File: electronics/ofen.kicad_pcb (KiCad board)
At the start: 2 copper layers, 100.3 x 76.2 mm, 61 parts, among them J1 motor, J2 DC, J3 AC_IN, J4 AC_OUT, J5 AC_OUT, Q1 Q_NPN_CBE, Q2 Q_NPN_CBE, Q3 Q_NPN_CBE, Q4 Q_NPN_CBE, Q5 BTA16-600B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

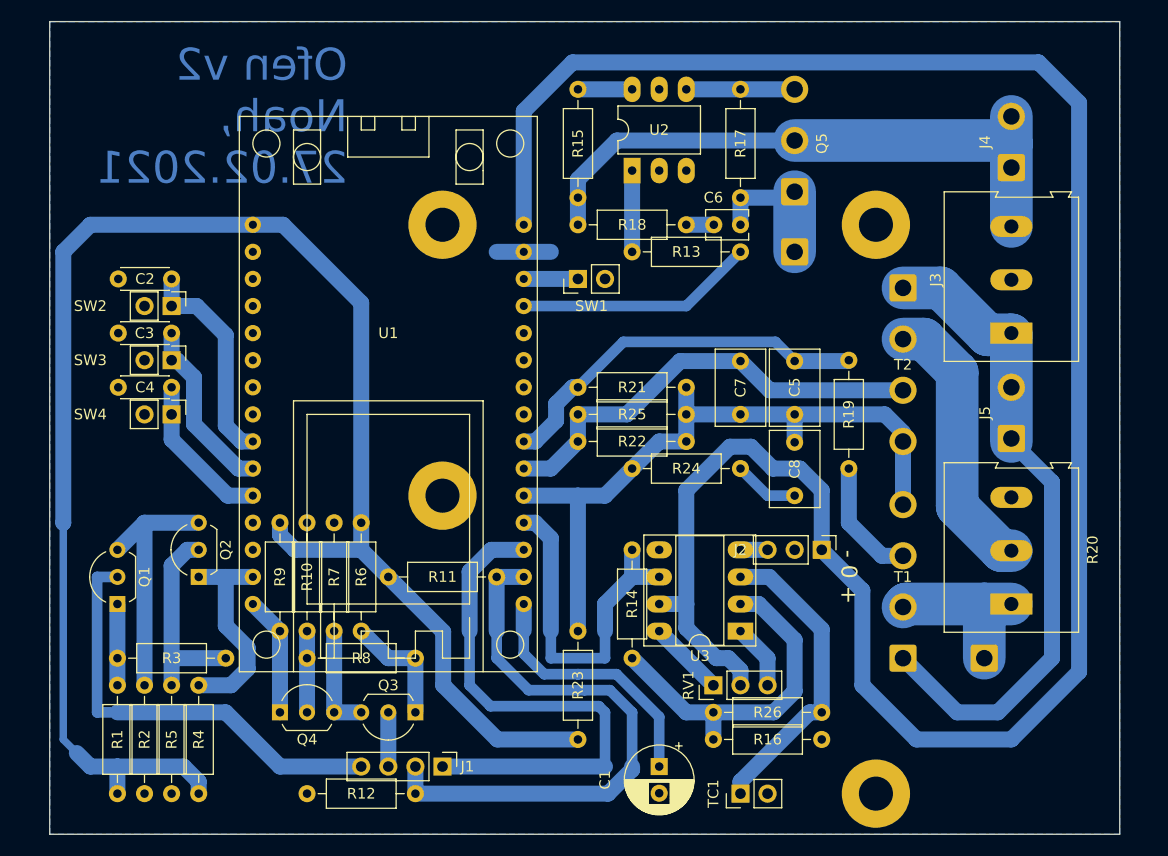
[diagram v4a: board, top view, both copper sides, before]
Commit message: added cold junction compensation and three status leds
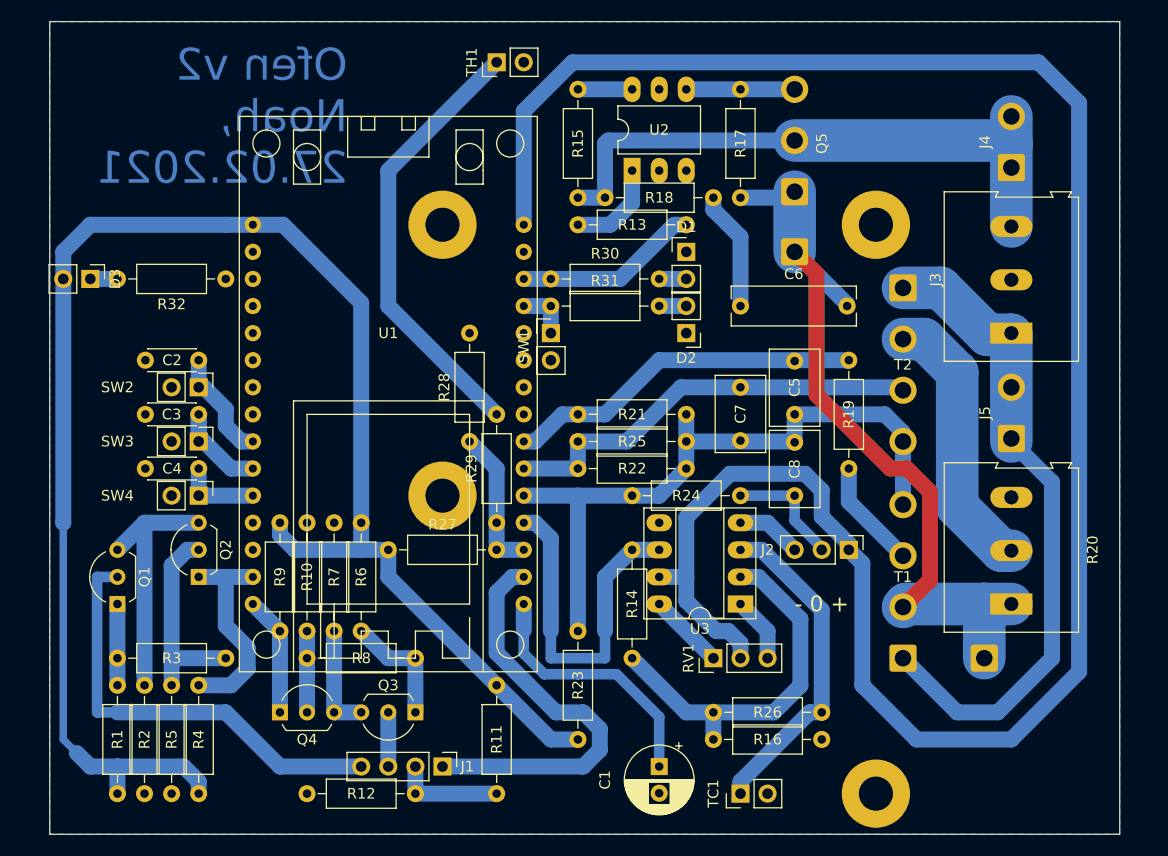
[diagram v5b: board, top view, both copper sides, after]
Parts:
- added D1: LED_heating, Connector_PinHeader_2.54mm:PinHeader_1x02_P2.54mm_Vertical, F.Cu at (177.8, 78.7)
- added D2: LED_running, Connector_PinHeader_2.54mm:PinHeader_1x02_P2.54mm_Vertical, F.Cu at (177.8, 86.4)
- added D3: LED_on, Connector_PinHeader_2.54mm:PinHeader_1x02_P2.54mm_Vertical, F.Cu at (121.9, 81.3)
- added R27: 15k, Resistor_THT:R_Axial_DIN0207_L6.3mm_D2.5mm_P10.16mm_Horizontal, F.Cu at (149.9, 106.7)
- added R28: 6.8k, Resistor_THT:R_Axial_DIN0207_L6.3mm_D2.5mm_P10.16mm_Horizontal, F.Cu at (157.5, 96.5)
- added R29: 330, Resistor_THT:R_Axial_DIN0207_L6.3mm_D2.5mm_P10.16mm_Horizontal, F.Cu at (160.0, 104.1)
- added R30: 68, Resistor_THT:R_Axial_DIN0207_L6.3mm_D2.5mm_P10.16mm_Horizontal, F.Cu at (165.1, 81.3)
- added R31: 68, Resistor_THT:R_Axial_DIN0207_L6.3mm_D2.5mm_P10.16mm_Horizontal, F.Cu at (165.1, 83.8)
- added R32: 68, Resistor_THT:R_Axial_DIN0207_L6.3mm_D2.5mm_P10.16mm_Horizontal, F.Cu at (134.6, 81.3)
- added TH1: 100k, Connector_PinHeader_2.54mm:PinHeader_1x02_P2.54mm_Vertical, F.Cu at (160.0, 61.0)
- C6: footprint Capacitor_THT:C_Disc_D3.8mm_W2.6mm_P2.50mm -> Capacitor_THT:C_Rect_L11.5mm_W3.5mm_P10.00mm_MKT
- R26: value 15k -> 3.3k
- moved R11 14.4 mm to (160.0, 119.4), turned to 270 degrees
- moved SW2 8.03 mm to (132.1, 91.4)
- moved C2 8.03 mm to (127.1, 88.9)
- moved C3 8.03 mm to (127.1, 94.0)
- moved C4 8.03 mm to (127.1, 99.1)
- moved SW3 8.03 mm to (132.1, 96.5)
- moved SW4 8.03 mm to (132.1, 101.6)
- moved C6 8.02 mm to (182.9, 83.8)
- moved R13 5.68 mm to (167.6, 76.2)
- moved SW1 5.68 mm to (165.1, 86.4), turned to 0 degrees
- moved R18 3.59 mm to (170.2, 73.7)
- moved R21 2.54 mm to (167.6, 94.0)
- moved R22 2.54 mm to (177.8, 99.1)
- moved J2 2.54 mm to (193.0, 106.7)
- moved R24 2.54 mm to (172.7, 101.6)
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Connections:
- SW1 pad 1: Net-(SW1-Pad1) -> Net-(R31-Pad1)
- U1 pad 17: Net-(J1-Pad2) -> Net-(J1-Pad1)
- U1 pad 18: Net-(J1-Pad1) -> Net-(R27-Pad2)
- U1 pad 27: Net-(R13-Pad2) -> Net-(R31-Pad1)
- U1 pad 28: Net-(SW1-Pad1) -> Net-(R13-Pad2)
- U1 pad 3: GND -> Net-(U1-Pad3)
- U1 pad 4: GND -> Net-(U1-Pad4)
- U1 pad 5: GND -> Net-(U1-Pad5)
- U1 pad 8: Net-(U1-Pad8) -> GND
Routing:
- net Net-(C6-Pad2): track 28.8 -> 73.9 mm
- net Net-(J1-Pad2): track 54.1 -> 10.2 mm
- net Net-(R29-Pad2): track 0.00 -> 41.4 mm
- net Net-(R27-Pad2): track 0.00 -> 13.8 mm
- net Net-(J1-Pad1): track 50.7 -> 38.8 mm
- net Net-(C2-Pad2): track 20.4 -> 10.6 mm
- net Net-(C6-Pad1): track 2.58 -> 11.2 mm
- net Net-(C4-Pad2): track 14.7 -> 7.62 mm
- net +5V: track 204.1 -> 198.0 mm
- net Net-(C3-Pad2): track 16.9 -> 10.9 mm
- net Net-(R31-Pad1): track 0.00 -> 5.08 mm
- net Net-(R13-Pad2): track 22.4 -> 17.3 mm
- net Net-(SW1-Pad1): track 5.08 -> 0.00 mm
- net -5V: track 2.54 -> 6.13 mm
- net Net-(R14-Pad1): track 32.0 -> 35.0 mm
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
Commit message: redesigned PCB. smaller, better, double layer
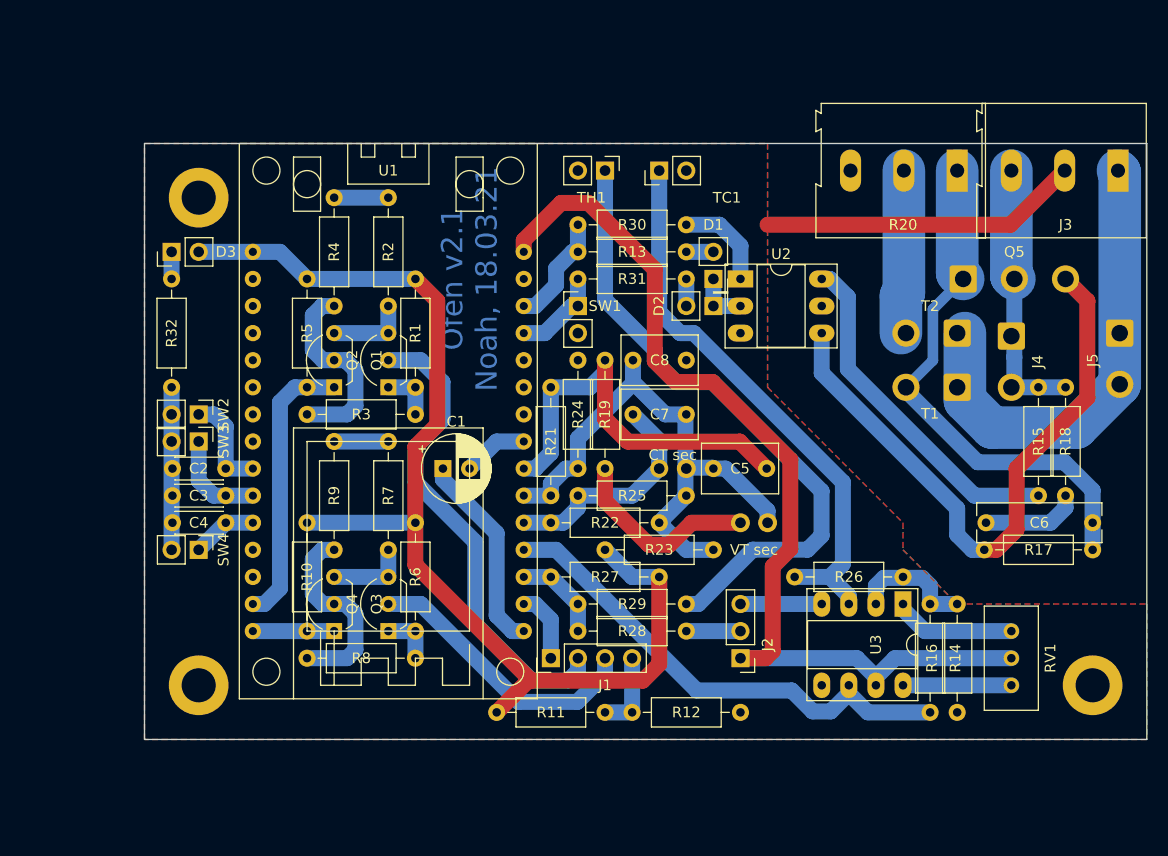
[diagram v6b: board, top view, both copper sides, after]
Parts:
- removed the   at (195.6, 129.5)
- removed the   at (154.9, 101.6)
- removed the   at (154.9, 76.2)
- removed the   at (195.6, 76.2)
- removed the   at (205.7, 116.8)
- removed the   at (188.0, 78.7)
- added  : , MountingHole:MountingHole_3.2mm_M3_DIN965_Pad, F.Cu at (132.1, 73.7)
- added  : , MountingHole:MountingHole_3.2mm_M3_DIN965_Pad, F.Cu at (215.9, 119.4)
- added  : , MountingHole:MountingHole_3.2mm_M3_DIN965_Pad, F.Cu at (132.1, 119.4)
- added ?: , , F.Cu at (182.9, 106.7)
- RV1: footprint Connector_PinHeader_2.54mm:PinHeader_1x03_P2.54mm_Vertical -> Potentiometer_THT:Potentiometer_Bourns_3296W_Vertical
- U2: footprint Package_DIP:DIP-6_W7.62mm_LongPads -> Package_DIP:DIP-6_W7.62mm_Socket_LongPads
- moved TC1 58.9 mm to (175.3, 71.1)
- moved R1 55.8 mm to (152.4, 81.3), turned to 270 degrees
- moved R5 49.3 mm to (142.2, 81.3), turned to 270 degrees
- moved R17 46.7 mm to (215.9, 106.7), turned to 180 degrees
- moved R15 46.7 mm to (210.8, 91.4), turned to 270 degrees
- moved R18 46.7 mm to (213.4, 91.4), turned to 270 degrees
- moved R2 42.3 mm to (149.9, 83.8), turned to 90 degrees
- moved R20 41.0 mm to (203.2, 71.1), turned to 180 degrees
- moved R4 38.7 mm to (144.8, 83.8), turned to 90 degrees
- moved C1 34.5 mm to (155.0, 99.1), turned to 0 degrees
- moved Q1 32.5 mm to (149.9, 91.4)
- moved C6 30.7 mm to (205.9, 104.1)
- moved R14 28.4 mm to (200.7, 111.8), turned to 270 degrees
- moved RV1 28.1 mm to (208.3, 119.4), turned to 270 degrees
- moved T1 25.9 mm to (203.2, 91.4), turned to 180 degrees
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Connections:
- Q1 pad 2: Net-(J1-Pad4) -> Net-(J1-Pad2)
- R11 pad 2: Net-(J1-Pad2) -> Net-(J1-Pad4)
- R12 pad 1: Net-(J1-Pad2) -> Net-(J1-Pad4)
- U1 pad 20: Net-(C5-Pad1) -> Net-(C7-Pad2)
- U1 pad 21: Net-(C7-Pad2) -> Net-(C5-Pad1)
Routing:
- net +5V: track 198.0 -> 92.1 mm
- net GND: track 11.2 -> 71.7 mm
- net +3V3: track 157.4 -> 106.8 mm
- net Net-(Q5-Pad3): track 10.2 -> 58.2 mm
- net Net-(J1-Pad2): track 10.2 -> 45.4 mm
- net Net-(J1-Pad4): track 40.8 -> 7.62 mm
- net Net-(J1-Pad1): track 38.8 -> 6.76 mm
- net Net-(J3-Pad3): track 56.3 -> 25.6 mm
- net Net-(R15-Pad2): track 5.08 -> 32.7 mm
- net Net-(C6-Pad2): track 73.9 -> 50.0 mm
- net Net-(R14-Pad1): track 35.0 -> 11.7 mm
- net Net-(R26-Pad2): track 31.0 -> 53.1 mm
- net Net-(J1-Pad3): track 5.08 -> 26.7 mm
- net Net-(C7-Pad2): track 40.3 -> 21.6 mm
- net Net-(R29-Pad2): track 41.4 -> 60.0 mm
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- added copper zone on F.Cu, net GND
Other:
- board size 100.3 x 76.2 mm -> 94 x 55.9 mm
- net class GND added: clearance 0.8, trace_width 0.7, via_dia 0.8, via_drill 0.4
- net class dick removed
- net class dünn removed
- net class mittel removed
- board text added: "CT sec"
- board text added: "Ofen v2.1 Noah, 18.03.21"
- board text added: "VT sec"
- board text removed: "- 0 +"
- board text removed: "Ofen v2 Noah, 27.02.2021"

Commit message: removed front GND pour on PCB
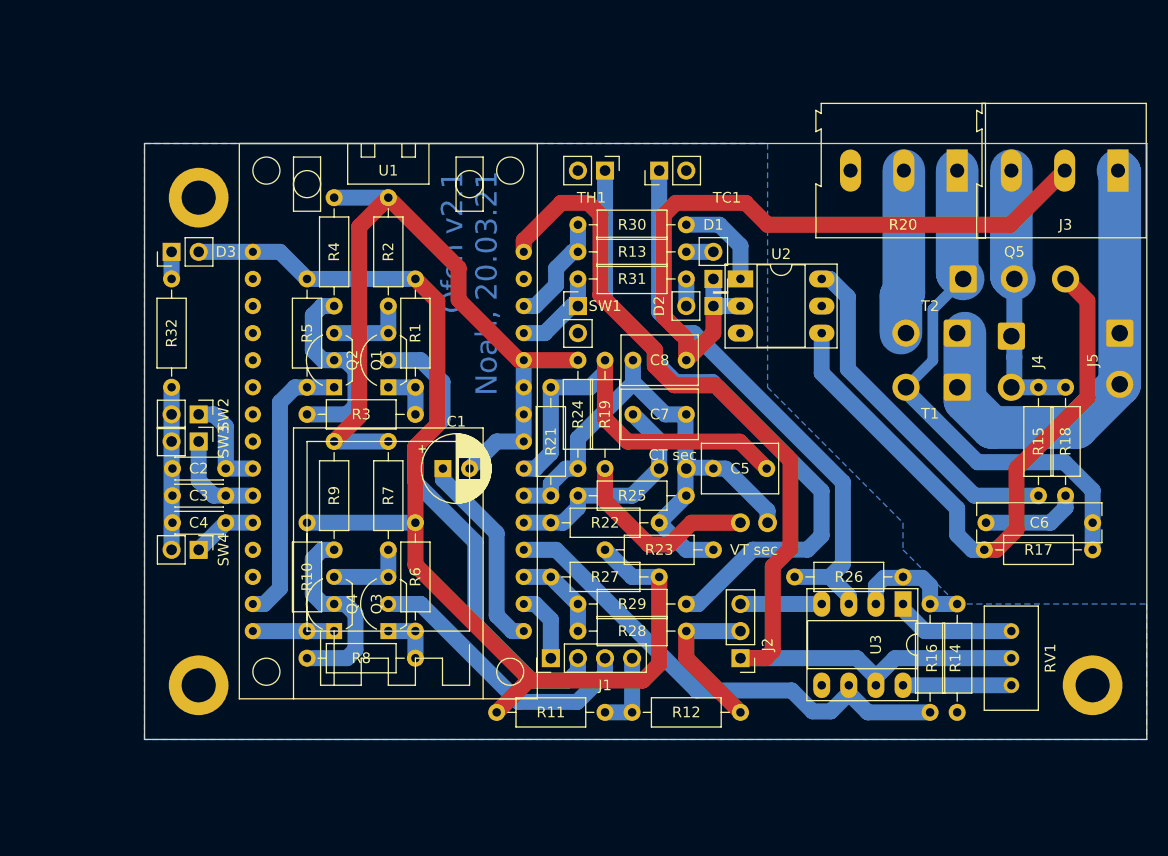
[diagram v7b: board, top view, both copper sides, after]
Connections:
- U1 pad 8: GND -> Net-(U1-Pad8)
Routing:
- net GND: track 71.7 -> 171.5 mm
- removed copper zone on F.Cu, net GND
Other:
- net class Default: clearance 0.5 -> 0.8
- net class GND: clearance 0.8 -> 0.5
- rule trace_clearance: 0.5 -> 0.8
- board text added: "Ofen v2.1 Noah, 20.03.21"
- board text removed: "Ofen v2.1 Noah, 18.03.21"
